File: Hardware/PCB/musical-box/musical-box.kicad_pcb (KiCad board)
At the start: 4 copper layers, 70 x 60 mm, 184 parts, among them J1 power, J201 PSU, J202 Jack-DC, J203 Li Ion 2S, J401 SPI Display, J402 Rotary Encoder 1, J403 I2C Display, J404 Rotary Encoder 2, J405 WS2812, J501 spk_out, J502 aux in, J503 line in, P201 USB_C, P202 ICT-Point, P203 ICT-Point, P204 ICT-Point, Q201 DMP3017SFK, Q204 IRF9362, Q301 BC846BDW1, SW301 boot, SW302 reset, U201 STUSB4500QTR, U202 MP2615, U203 TPS56339, U204 TLV75733PDBV, U205 TLV75733PDBV, U206 TLV803EC30DBZR, U301 CH340C, U302 ESP32-WROVER, U401 PCF8574ATS, U501 SPH0644HM4H-1, U502 SPH0644HM4H-1, U503 TAS5754MDCA

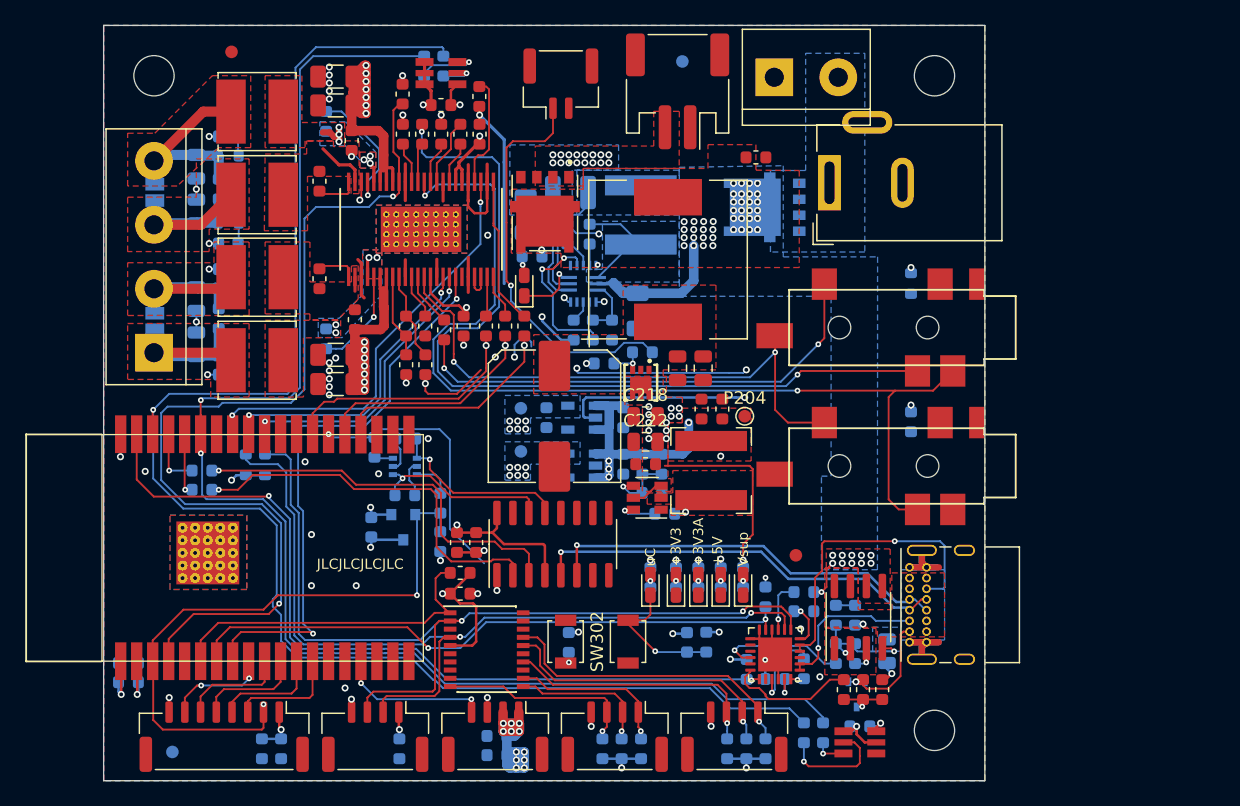
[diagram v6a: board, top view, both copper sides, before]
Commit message: Route aux and line detect
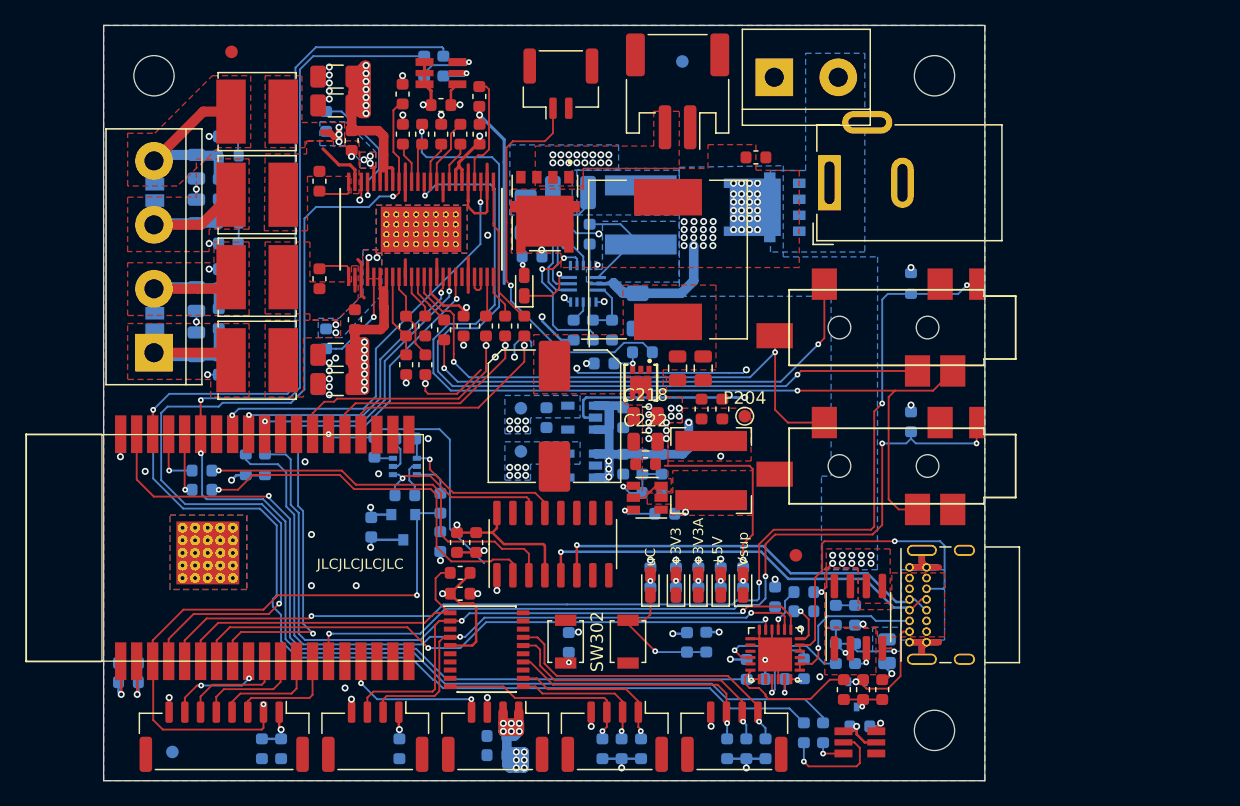
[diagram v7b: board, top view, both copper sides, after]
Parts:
- moved R214 0.76 mm to (403.3, 170.4)
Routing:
- net /Audio Output/AUX_Detect: track 0.00 -> 89.0 mm, vias 0 -> 4
- net /Microcontroller/IO12: track 0.00 -> 68.7 mm, vias 0 -> 4
- net /Microcontroller/I35: track 49.1 -> 48.2 mm
- net Net-(R210-Pad2): track 4.09 -> 3.51 mm
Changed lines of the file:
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@@
     (thickness 1.6)
     (drawings 12)
-    (tracks 1656)
+    (tracks 1710)
     (zones 0)
     (modules 184)
@@
   (layers
     (0 F.Cu signal)
-    (1 In1.Cu signal hide)
+    (1 In1.Cu signal)
     (2 In2.Cu signal hide)
     (31 B.Cu signal)
@@
     (44 Edge.Cuts user)
     (45 Margin user hide)
-    (46 B.CrtYd user hide)
+    (46 B.CrtYd user)
     (47 F.CrtYd user hide)
     (48 B.Fab user hide)
@@
   )
   (module Resistor_SMD:R_0603_1608Metric (layer B.Cu)
-    (at 402.578 170.395 270)
+    (at 403.34 170.395 270)
     (descr "Resistor SMD 0603 (1608 Metric), square (rectangular) end terminal, IPC_7351 nominal, (Body size source: http://www.tortai-tech.com/upload/download/2011102023233369053.pdf), generated with kicad-footprint-generator")
     (tags resistor)
@@
   (segment (start 373.45 180.891) (end 373.495 180.936) (width 0.2) (layer F.Cu) (net 3))
   (segment (start 373.495 180.936) (end 373.495 181.6725) (width 0.2) (layer B.Cu) (net 3))
-  (via (at 402.578 168.871) (size 0.46) (drill 0.2) (layers F.Cu B.Cu) (net 3))
-  (segment (start 402.578 169.6075) (end 402.578 168.871) (width 0.15) (layer B.Cu) (net 3))
   (segment (start 397.887 173.189) (end 397.872 173.204) (width 0.2) (layer B.Cu) (net 3))
   (segment (start 398.895 173.189) (end 397.887 173.189) (width 0.2) (layer B.Cu) (net 3))
@@
   (segment (start 376.743 167.498674) (end 376.757663 167.513337) (width 0.2) (layer B.Cu) (net 3))
   (segment (start 376.743 166.7915) (end 376.743 167.498674) (width 0.2) (layer B.Cu) (net 3))
+  (via (at 403.34 168.998) (size 0.56) (drill 0.3) (layers F.Cu B.Cu) (net 3))
+  (segment (start 403.34 169.6075) (end 403.34 168.998) (width 0.2) (layer B.Cu) (net 3))
   (segment (start 375.965801 144.971501) (end 375.965801 146.242469) (width 0.2) (layer F.Cu) (net 4))
   (segment (start 375.965801 146.242469) (end 376.977332 147.254) (width 0.2) (layer F.Cu) (net 4))
@@
   (segment (start 403.59 173.0045) (end 403.59 172.177) (width 0.15) (layer F.Cu) (net 83))
   (segment (start 403.59 172.177) (end 403.594 172.173) (width 0.15) (layer F.Cu) (net 83))
-  (segment (start 403.594 172.173) (end 403.594 170.268) (width 0.15) (layer B.Cu) (net 83))
-  (segment (start 403.848 170.014) (end 404.8385 170.014) (width 0.15) (layer B.Cu) (net 83))
-  (segment (start 403.594 170.268) (end 403.848 170.014) (width 0.15) (layer B.Cu) (net 83))
+  (segment (start 404.12599 170.72651) (end 404.8385 170.014) (width 0.15) (layer B.Cu) (net 83))
+  (segment (start 404.12599 171.64101) (end 404.12599 170.72651) (width 0.15) (layer B.Cu) (net 83))
+  (segment (start 403.594 172.173) (end 404.12599 171.64101) (width 0.15) (layer B.Cu) (net 83))
   (via (at 386.573152 143.482411) (size 0.46) (drill 0.2) (layers F.Cu B.Cu) (net 84))
   (segment (start 386.631564 143.423999) (end 386.573152 143.482411) (width 0.15) (layer B.Cu) (net 84))
@@
   (segment (start 402.59 173.0045) (end 402.59 172.185) (width 0.15) (layer F.Cu) (net 95))
   (segment (start 402.59 172.185) (end 402.578 172.173) (width 0.15) (layer F.Cu) (net 95))
-  (segment (start 402.578 172.173) (end 402.578 171.1825) (width 0.15) (layer B.Cu) (net 95))
   (via (at 375.781 174.459) (size 0.46) (drill 0.2) (layers F.Cu B.Cu) (net 95))
   (segment (start 402.348001 172.402999) (end 402.578 172.173) (width 0.15) (layer B.Cu) (net 95))
@@
   (segment (start 375.273 135.089) (end 375.654 135.47) (width 0.15) (layer B.Cu) (net 147))
   (segment (start 375.273 133.438) (end 375.273 135.089) (width 0.15) (layer B.Cu) (net 147))
+  (segment (start 356.437 173.854) (end 358.18302 172.10798) (width 0.15) (layer F.Cu) (net 148))
+  (segment (start 356.437 175.504) (end 356.437 173.854) (width 0.15) (layer F.Cu) (net 148))
+  (via (at 366.51 171.919) (size 0.46) (drill 0.2) (layers F.Cu B.Cu) (net 148))
+  (segment (start 366.32102 172.10798) (end 366.51 171.919) (width 0.15) (layer F.Cu) (net 148))
+  (segment (start 358.18302 172.10798) (end 366.32102 172.10798) (width 0.15) (layer F.Cu) (net 148))
+  (segment (start 366.51 171.919) (end 376.061024 171.919) (width 0.15) (layer B.Cu) (net 148))
+  (segment (start 376.061024 171.919) (end 376.984054 170.99597) (width 0.15) (layer B.Cu) (net 148))
+  (segment (start 376.984054 170.99597) (end 386.83 170.99597) (width 0.15) (layer B.Cu) (net 148))
+  (segment (start 399.958042 170.99597) (end 400.27346 170.680552) (width 0.15) (layer B.Cu) (net 148))
+  (segment (start 386.83 170.99597) (end 399.958042 170.99597) (width 0.15) (layer B.Cu) (net 148))
+  (segment (start 400.27346 170.680552) (end 401.911448 170.680552) (width 0.15) (layer B.Cu) (net 148))
+  (via (at 402.07 169.252) (size 0.46) (drill 0.2) (layers F.Cu B.Cu) (net 148))
+  (segment (start 402.07 170.522) (end 402.07 169.252) (width 0.15) (layer B.Cu) (net 148))
+  (segment (start 401.911448 170.680552) (end 402.07 170.522) (width 0.15) (layer B.Cu) (net 148))
+  (segment (start 402.07 166.217012) (end 403.226012 165.061) (width 0.15) (layer F.Cu) (net 148))
+  (segment (start 402.07 169.252) (end 402.07 166.217012) (width 0.15) (layer F.Cu) (net 148))
+  (segment (start 403.226012 165.061) (end 410.96 165.061) (width 0.15) (layer F.Cu) (net 148))
+  (segment (start 410.96 165.061) (end 411.214 164.807) (width 0.15) (layer F.Cu) (net 148))
+  (via (at 411.849 155.028) (size 0.46) (drill 0.2) (layers F.Cu B.Cu) (net 148))
+  (segment (start 411.214 155.663) (end 411.849 155.028) (width 0.15) (layer F.Cu) (net 148))
+  (segment (start 411.214 164.807) (end 411.214 155.663) (width 0.15) (layer F.Cu) (net 148))
+  (segment (start 412.294 146.328) (end 414.135 146.328) (width 0.15) (layer B.Cu) (net 148))
+  (segment (start 411.849 146.773) (end 412.294 146.328) (width 0.15) (layer B.Cu) (net 148))
+  (segment (start 411.849 155.028) (end 411.849 146.773) (width 0.15) (layer B.Cu) (net 148))
+  (via (at 418.58 145.63) (size 0.46) (drill 0.2) (layers F.Cu B.Cu) (net 148))
+  (segment (start 417.882 146.328) (end 418.58 145.63) (width 0.15) (layer B.Cu) (net 148))
+  (segment (start 414.135 146.328) (end 417.882 146.328) (width 0.15) (layer B.Cu) (net 148))
+  (segment (start 419.2716 145.63) (end 419.3516 145.55) (width 0.15) (layer F.Cu) (net 148))
+  (segment (start 418.58 145.63) (end 419.2716 145.63) (width 0.15) (layer F.Cu) (net 148))
   (segment (start 385.697 131.578) (end 385.697 133.555) (width 0.15) (layer F.Cu) (net 149))
   (segment (start 385.697 133.555) (end 385.052 134.2) (width 0.15) (layer F.Cu) (net 149))
@@
   (segment (start 390.582784 150.964) (end 386.449 150.964) (width 0.15) (layer B.Cu) (net 149))
   (segment (start 382.353174 146.868174) (end 386.449 150.964) (width 0.15) (layer B.Cu) (net 149))
+  (via (at 367.907 173.316001) (size 0.46) (drill 0.2) (layers F.Cu B.Cu) (net 150))
+  (segment (start 367.867 173.356001) (end 367.907 173.316001) (width 0.15) (layer F.Cu) (net 150))
+  (segment (start 367.867 175.504) (end 367.867 173.356001) (width 0.15) (layer F.Cu) (net 150))
+  (via (at 402.578 168.766) (size 0.46) (drill 0.2) (layers F.Cu B.Cu) (net 150))
+  (segment (start 402.578 170.522) (end 402.578 168.766) (width 0.15) (layer B.Cu) (net 150))
+  (segment (start 400.418438 171.030562) (end 402.069438 171.030562) (width 0.15) (layer B.Cu) (net 150))
+  (segment (start 400.10302 171.34598) (end 400.418438 171.030562) (width 0.15) (layer B.Cu) (net 150))
+  (segment (start 402.069438 171.030562) (end 402.578 170.522) (width 0.15) (layer B.Cu) (net 150))
+  (segment (start 377.129032 171.34598) (end 400.10302 171.34598) (width 0.15) (layer B.Cu) (net 150))
+  (segment (start 375.159012 173.316) (end 377.129032 171.34598) (width 0.15) (layer B.Cu) (net 150))
+  (segment (start 368.23227 173.316) (end 375.159012 173.316) (width 0.15) (layer B.Cu) (net 150))
+  (segment (start 367.907 173.316001) (end 368.23227 173.316) (width 0.15) (layer B.Cu) (net 150))
+  (via (at 419.342 158.203) (size 0.46) (drill 0.2) (layers F.Cu B.Cu) (net 150))
+  (segment (start 419.3516 158.1934) (end 419.342 158.203) (width 0.15) (layer F.Cu) (net 150))
+  (segment (start 419.3516 156.55) (end 419.3516 158.1934) (width 0.15) (layer F.Cu) (net 150))
+  (segment (start 414.135 157.822) (end 414.135 157.276) (width 0.15) (layer B.Cu) (net 150))
+  (segment (start 414.516 158.203) (end 414.135 157.822) (width 0.15) (layer B.Cu) (net 150))
+  (segment (start 419.342 158.203) (end 414.516 158.203) (width 0.15) (layer B.Cu) (net 150))
+  (via (at 411.849 158.203) (size 0.46) (drill 0.2) (layers F.Cu B.Cu) (net 150))
+  (segment (start 413.754 158.203) (end 411.849 158.203) (width 0.15) (layer B.Cu) (net 150))
+  (segment (start 414.135 157.822) (end 413.754 158.203) (width 0.15) (layer B.Cu) (net 150))
+  (segment (start 411.849 158.203) (end 411.849 164.68) (width 0.15) (layer F.Cu) (net 150))
+  (segment (start 411.849 164.68) (end 411.087 165.442) (width 0.15) (layer F.Cu) (net 150))
+  (segment (start 411.087 165.442) (end 403.34 165.442) (width 0.15) (layer F.Cu) (net 150))
+  (segment (start 402.578 166.204) (end 402.578 168.766) (width 0.15) (layer F.Cu) (net 150))
+  (segment (start 403.34 165.442) (end 402.578 166.204) (width 0.15) (layer F.Cu) (net 150))
   (zone (net 1) (net_name GND) (layer In2.Cu) (hatch edge 0.508)
     (connect_pads thru_hole_only (clearance 0.2))

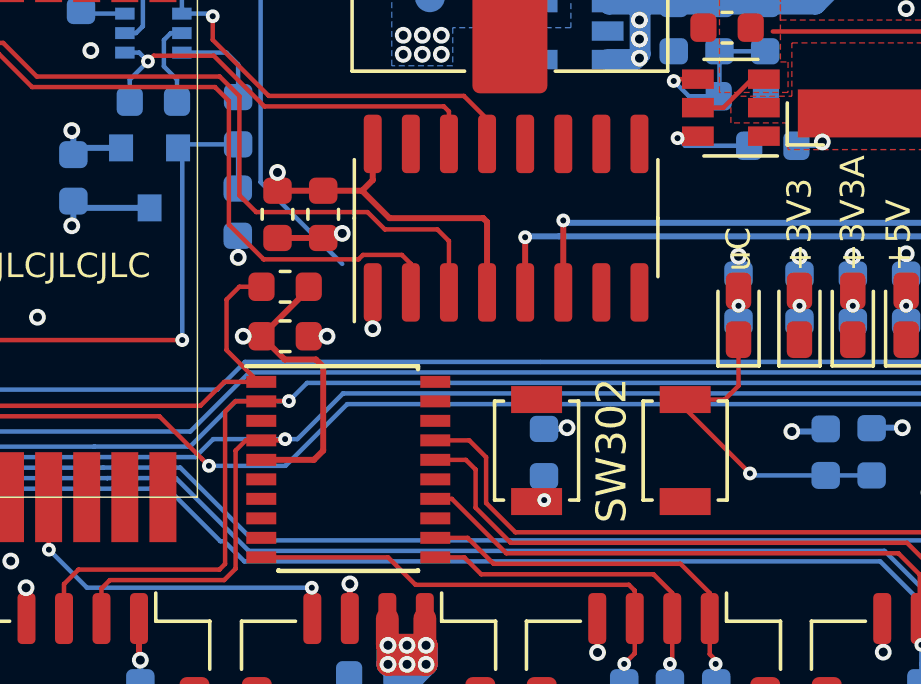
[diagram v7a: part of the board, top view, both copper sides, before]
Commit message: Route Reset and IO0 stubs
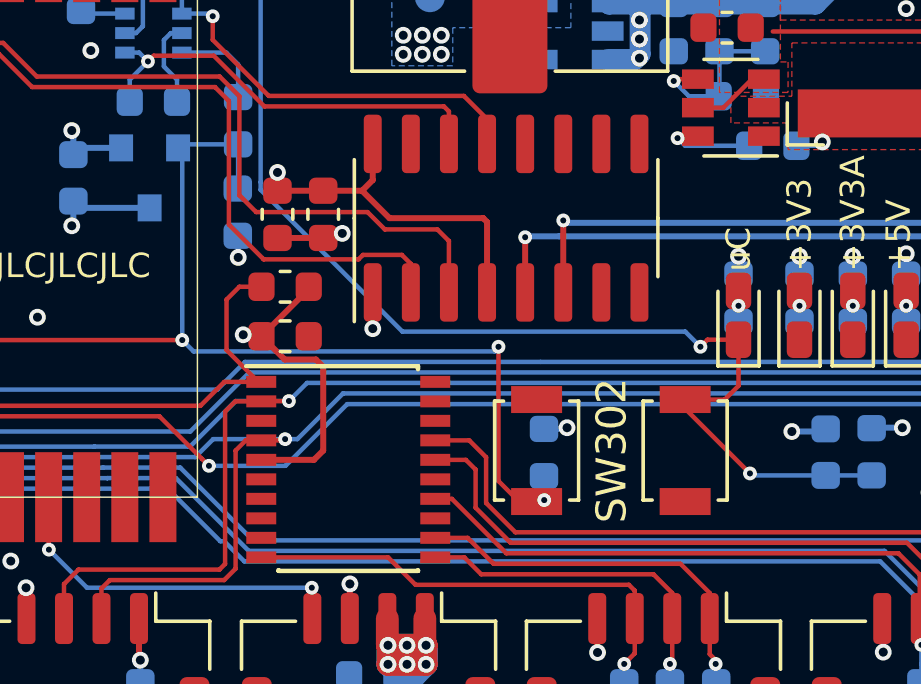
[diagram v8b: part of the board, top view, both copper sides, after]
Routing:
- net /Microcontroller/~RESET: track 51.1 -> 67.9 mm, vias 3 -> 4
- net /Microcontroller/IO00: track 32.5 -> 47.1 mm, vias 2 -> 3
- net GND: track 164.5 -> 163.8 mm, vias 63 -> 62
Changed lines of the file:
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@@
     (thickness 1.6)
     (drawings 12)
-    (tracks 1710)
+    (tracks 1723)
     (zones 0)
     (modules 184)
@@
   (segment (start 382.639 151.345) (end 382.639 150.376598) (width 0.15) (layer B.Cu) (net 1))
   (segment (start 383.975001 150.150599) (end 383.975001 150.5068) (width 0.15) (layer B.Cu) (net 1))
-  (via (at 379.718 170.141) (size 0.56) (drill 0.3) (layers F.Cu B.Cu) (net 1))
-  (segment (start 379.1085 170.141) (end 379.718 170.141) (width 0.2) (layer F.Cu) (net 1))
   (segment (start 378.067 166.8645) (end 379.591 166.8645) (width 0.2) (layer F.Cu) (net 1))
   (via (at 380.226 166.712) (size 0.56) (drill 0.3) (layers F.Cu B.Cu) (net 1))
@@
   (segment (start 378.30851 170.91601) (end 377.5335 170.141) (width 0.2) (layer F.Cu) (net 3))
   (segment (start 379.35001 170.91601) (end 378.30851 170.91601) (width 0.2) (layer F.Cu) (net 3))
-  (via (at 376.924 170.141) (size 0.56) (drill 0.3) (layers F.Cu B.Cu) (net 3))
-  (segment (start 377.5335 170.141) (end 376.924 170.141) (width 0.2) (layer F.Cu) (net 3))
   (segment (start 379.1085 168.566) (end 377.5335 170.141) (width 0.2) (layer F.Cu) (net 3))
   (segment (start 379.1085 168.49) (end 379.1085 168.566) (width 0.2) (layer F.Cu) (net 3))
@@
   (via (at 403.34 168.998) (size 0.56) (drill 0.3) (layers F.Cu B.Cu) (net 3))
   (segment (start 403.34 169.6075) (end 403.34 168.998) (width 0.2) (layer B.Cu) (net 3))
+  (via (at 376.923999 170.09096) (size 0.56) (drill 0.3) (layers F.Cu B.Cu) (net 3))
+  (segment (start 376.974039 170.141) (end 376.923999 170.09096) (width 0.2) (layer F.Cu) (net 3))
+  (segment (start 377.5335 170.141) (end 376.974039 170.141) (width 0.2) (layer F.Cu) (net 3))
   (segment (start 375.965801 144.971501) (end 375.965801 146.242469) (width 0.2) (layer F.Cu) (net 4))
   (segment (start 375.965801 146.242469) (end 376.977332 147.254) (width 0.2) (layer F.Cu) (net 4))
@@
   (segment (start 377.50501 157.89501) (end 377.50501 165.00701) (width 0.15) (layer B.Cu) (net 5))
   (segment (start 376.68199 157.07199) (end 377.50501 157.89501) (width 0.15) (layer B.Cu) (net 5))
-  (segment (start 377.50501 165.00701) (end 380.226 167.728) (width 0.15) (layer B.Cu) (net 5))
   (segment (start 391.656 172.554) (end 391.656 172.251) (width 0.15) (layer F.Cu) (net 5))
   (segment (start 393.815 174.713) (end 391.656 172.554) (width 0.15) (layer F.Cu) (net 5))
@@
   (segment (start 393.434 171.792) (end 393.434 170.255) (width 0.15) (layer F.Cu) (net 5))
   (segment (start 392.975 172.251) (end 393.434 171.792) (width 0.15) (layer F.Cu) (net 5))
+  (via (at 392.164 170.49097) (size 0.46) (drill 0.2) (layers F.Cu B.Cu) (net 5))
+  (segment (start 392.39997 170.255) (end 392.164 170.49097) (width 0.15) (layer F.Cu) (net 5))
+  (segment (start 393.434 170.255) (end 392.39997 170.255) (width 0.15) (layer F.Cu) (net 5))
+  (segment (start 377.50501 165.26101) (end 377.50501 165.00701) (width 0.15) (layer B.Cu) (net 5))
+  (segment (start 382.229969 169.985969) (end 377.50501 165.26101) (width 0.15) (layer B.Cu) (net 5))
+  (segment (start 391.658999 169.985969) (end 382.229969 169.985969) (width 0.15) (layer B.Cu) (net 5))
+  (segment (start 392.164 170.49097) (end 391.658999 169.985969) (width 0.15) (layer B.Cu) (net 5))
   (segment (start 383.42 149.6675) (end 383.42 150.417) (width 0.15) (layer F.Cu) (net 6))
   (via (at 383.42 150.417) (size 0.56) (drill 0.3) (layers F.Cu B.Cu) (net 6))
@@
   (segment (start 374.892 164) (end 374.753 163.861) (width 0.15) (layer B.Cu) (net 63))
   (segment (start 374.892 170.268) (end 374.892 164) (width 0.15) (layer B.Cu) (net 63))
+  (segment (start 386.703 175.651) (end 386.117 175.651) (width 0.15) (layer F.Cu) (net 63))
+  (via (at 385.433 170.49097) (size 0.46) (drill 0.2) (layers F.Cu B.Cu) (net 63))
+  (segment (start 385.433 174.967) (end 385.433 170.49097) (width 0.15) (layer F.Cu) (net 63))
+  (segment (start 386.117 175.651) (end 385.433 174.967) (width 0.15) (layer F.Cu) (net 63))
+  (segment (start 385.433 170.522) (end 385.30904 170.64596) (width 0.15) (layer B.Cu) (net 63))
+  (segment (start 385.433 170.49097) (end 385.433 170.522) (width 0.15) (layer B.Cu) (net 63))
+  (segment (start 375.26996 170.64596) (end 374.892 170.268) (width 0.15) (layer B.Cu) (net 63))
+  (segment (start 385.30904 170.64596) (end 375.26996 170.64596) (width 0.15) (layer B.Cu) (net 63))
   (via (at 389.624 181.063) (size 0.46) (drill 0.2) (layers F.Cu B.Cu) (net 64))
   (segment (start 389.624 181.6725) (end 389.624 181.063) (width 0.15) (layer B.Cu) (net 64))
